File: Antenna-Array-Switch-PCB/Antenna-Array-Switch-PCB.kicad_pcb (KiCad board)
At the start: 2 copper layers, 80 parts, among them J1 Conn_Coaxial, J2 Conn_Coaxial, J3 Conn_Coaxial, J4 Conn_SMA, SW1 TS-1187A-B-A-B, SW2 TS-1187A-B-A-B, U1 PGA-103, U2 TPS22917DBV, U3 TPS22917DBV, U4 PGA-103, U5 TPS22917DBV, U6 PGA-103, U7 SKY13418-485LF, U8 LM1117IMP-3.3, U9 RP2040-Zero

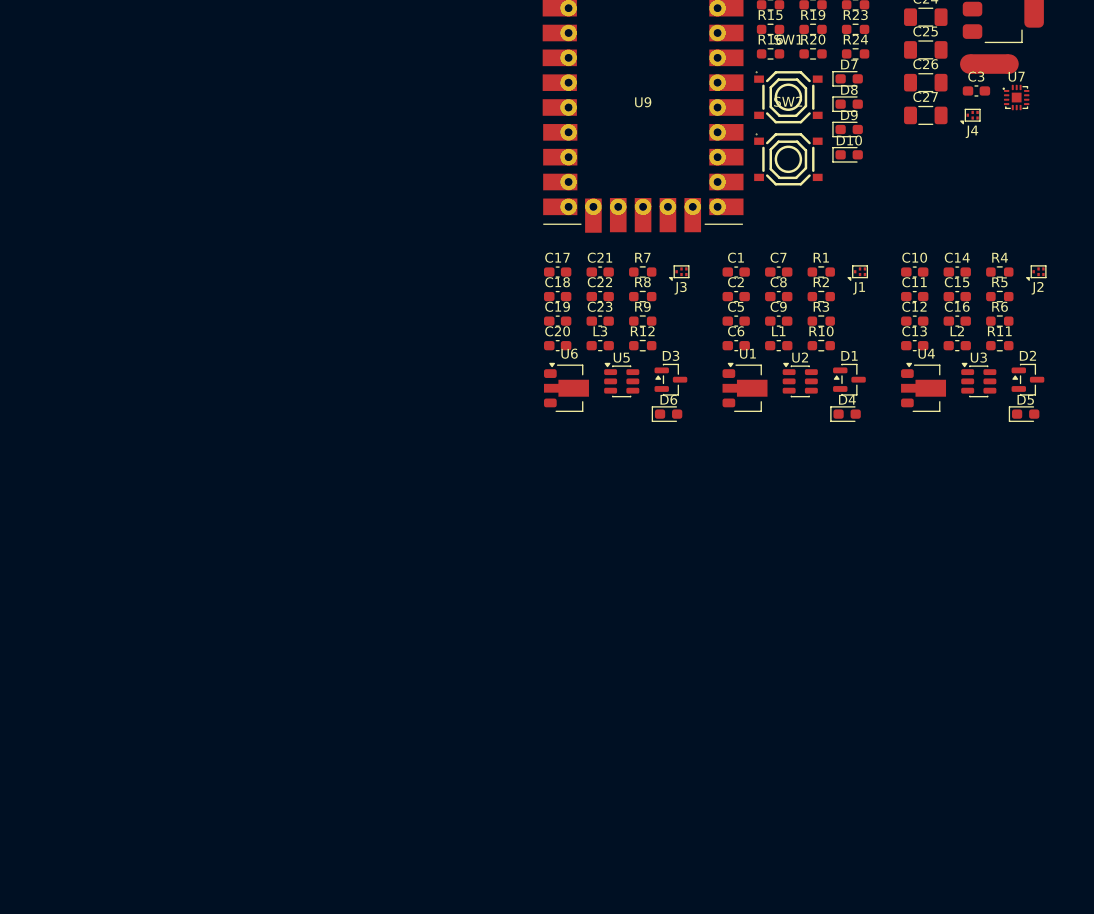
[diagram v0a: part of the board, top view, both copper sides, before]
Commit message: PCB: Layout an LNA segment
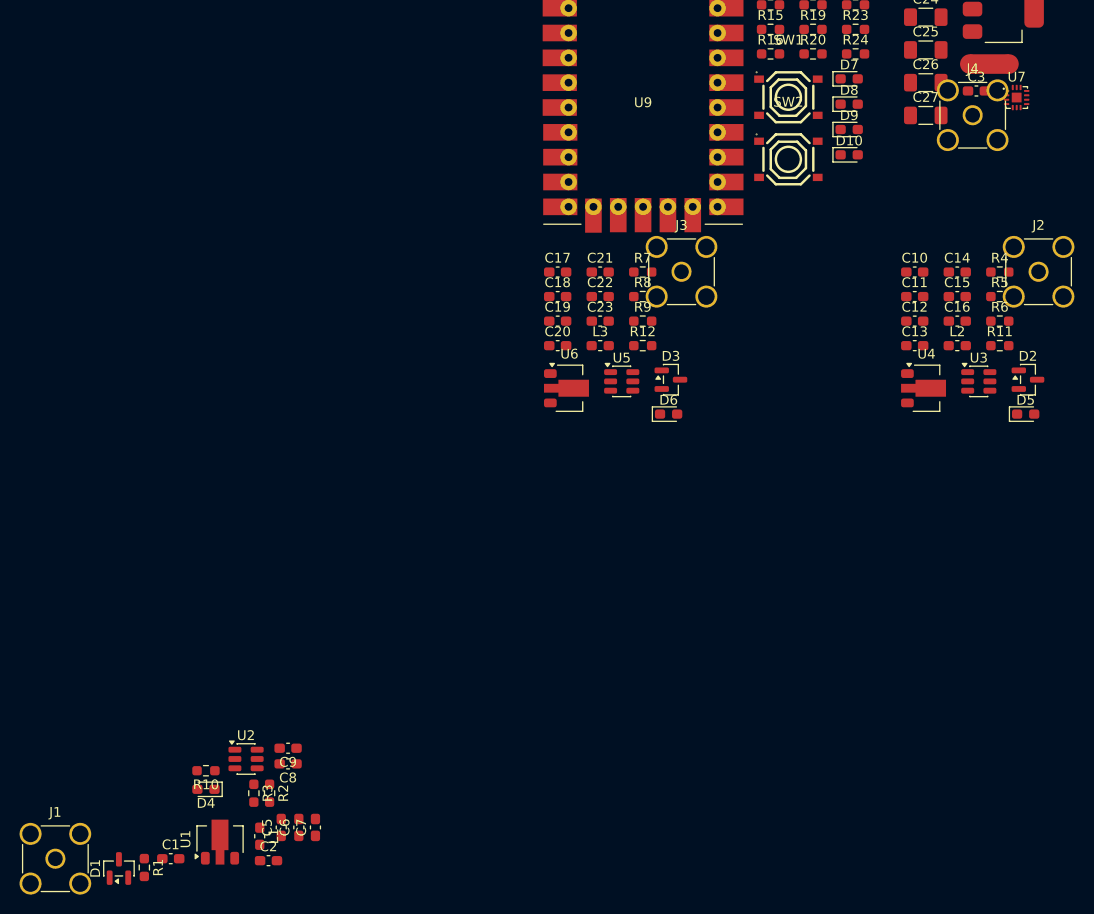
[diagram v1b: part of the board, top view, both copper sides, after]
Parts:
- J1, J2, J3, J4: footprint Filter:Filter_1411-5_1.4x1.1mm -> Connector_Coaxial:SMA_Amphenol_901-144_Vertical
- moved J1 101.9 mm to (63.3, 158.4)
- moved R1 92.2 mm to (72.4, 159.3), turned to -90 degrees
- moved D1 89.9 mm to (69.8, 159.4), turned to 90 degrees
- moved C1 83.3 mm to (75.1, 158.4)
- moved R10 76.5 mm to (78.7, 149.4), turned to 180 degrees
- moved D4 76.0 mm to (78.7, 151.3), turned to 180 degrees
- moved R2 75.9 mm to (85.2, 151.7), turned to -90 degrees
- moved R3 75.5 mm to (83.6, 151.7), turned to -90 degrees
- moved C2 74.9 mm to (85.1, 158.6)
- moved C7 74.0 mm to (89.9, 155.2), turned to 90 degrees
- moved L1 73.0 mm to (84.2, 156.1), turned to -90 degrees
- moved U1 71.0 mm to (80.1, 156.4), turned to 90 degrees
- moved C5 69.6 mm to (86.4, 155.2), turned to 90 degrees
- moved C8 69.3 mm to (87.1, 148.7), turned to 180 degrees
- moved U2 68.6 mm to (82.8, 148.2)
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
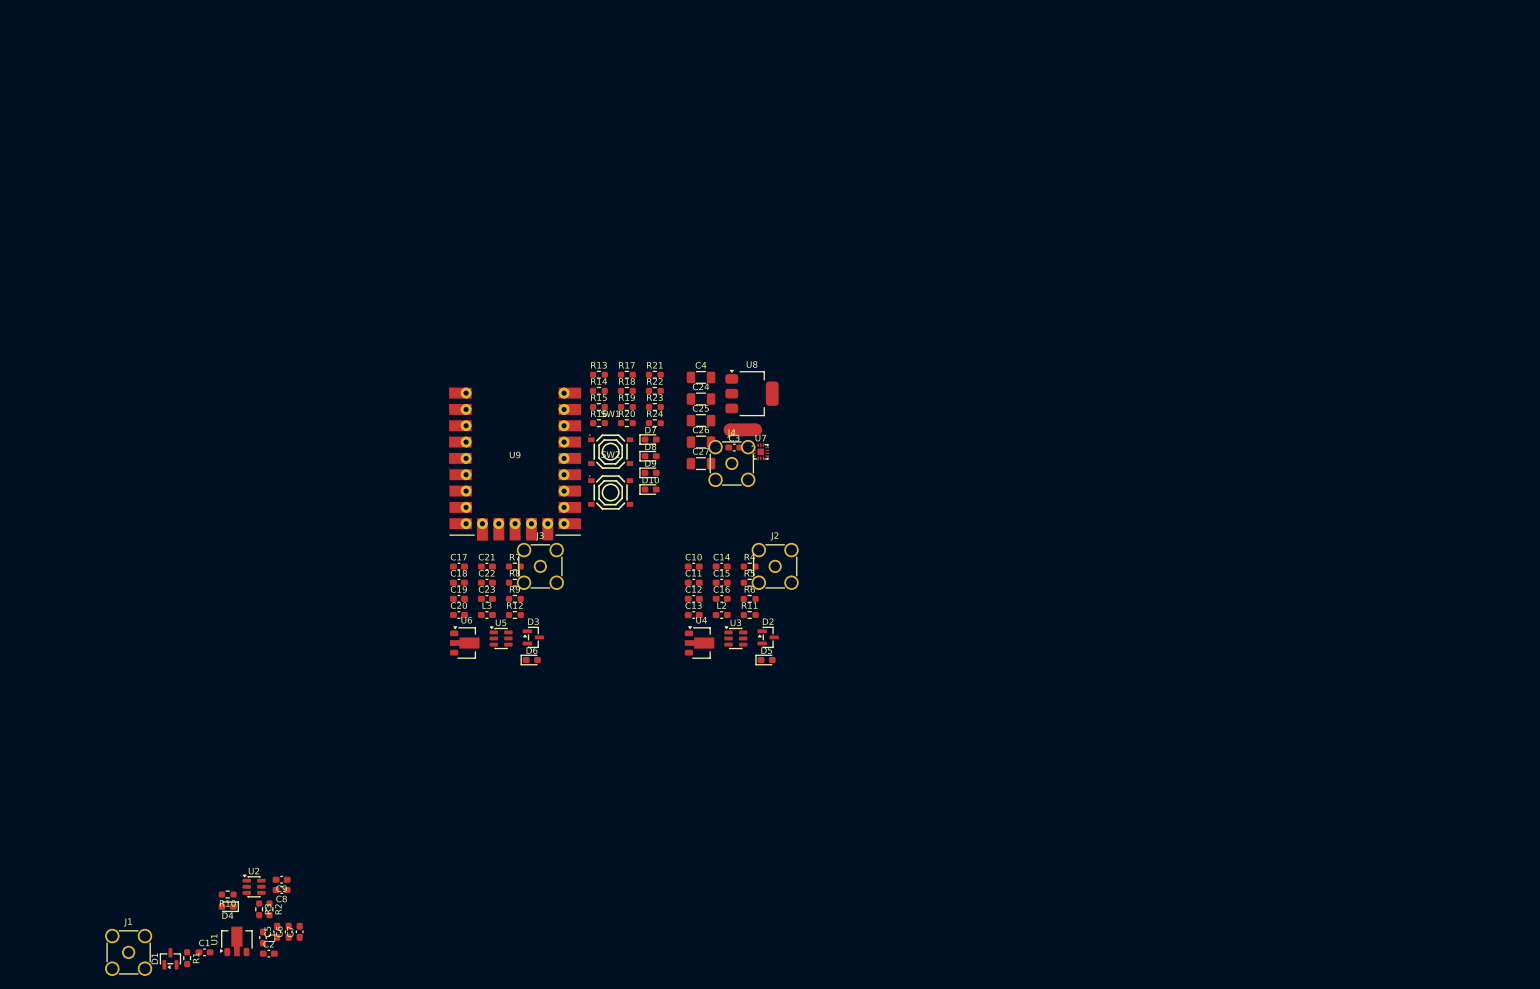
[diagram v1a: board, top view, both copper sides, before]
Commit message: PCB, Docs: Layout, stackup, shielding
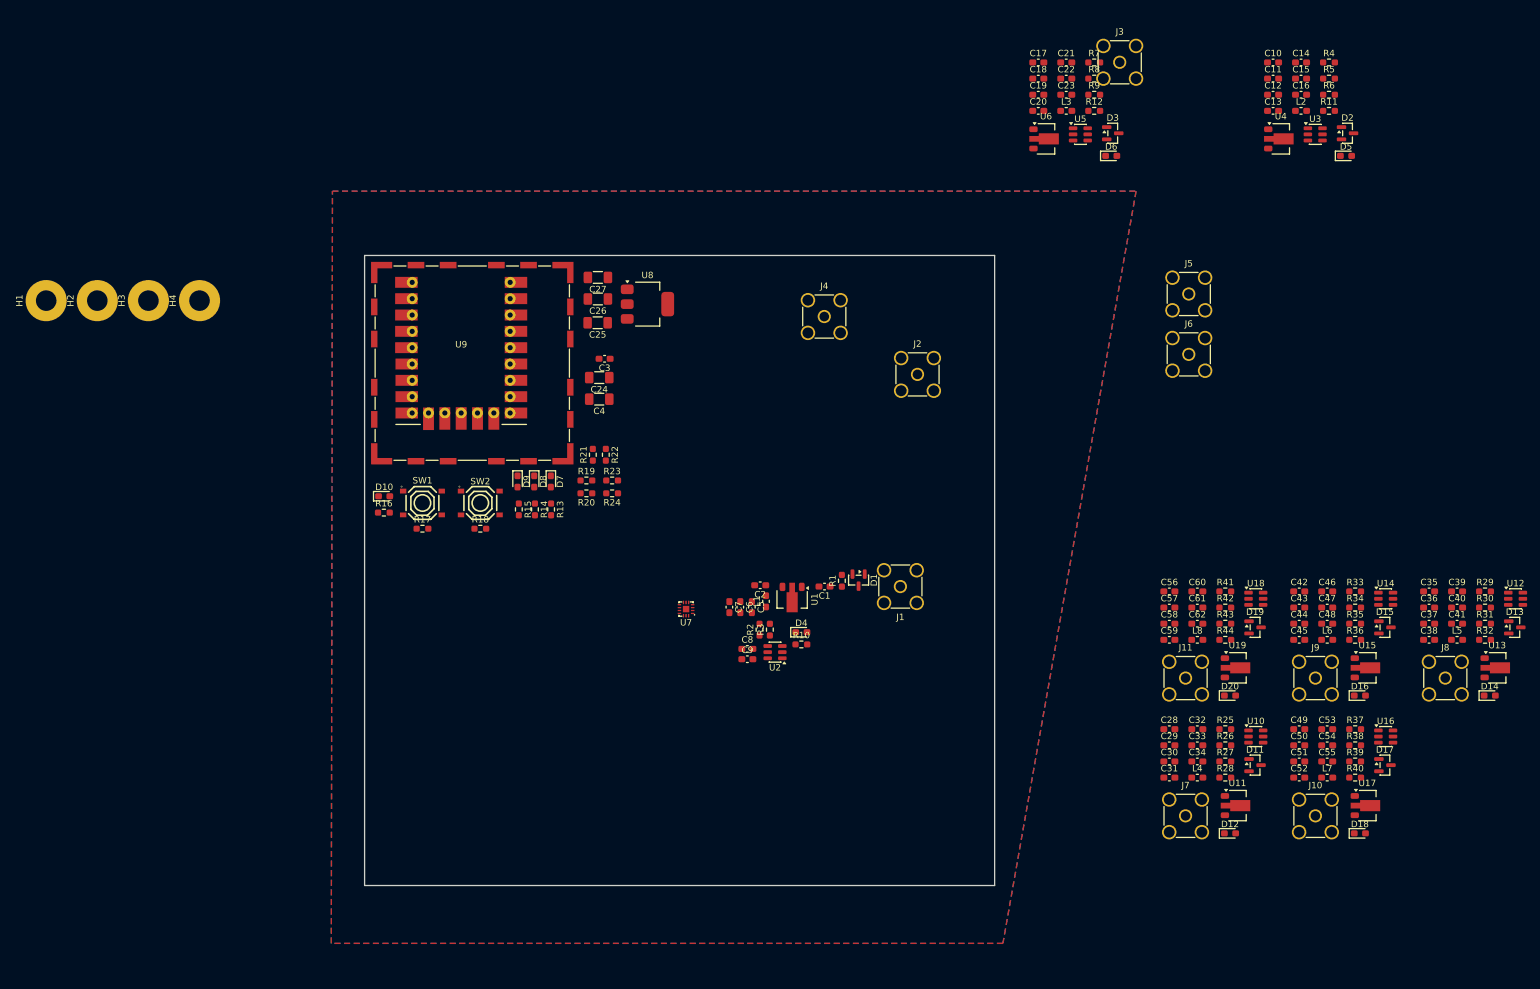
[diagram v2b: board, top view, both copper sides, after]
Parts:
- removed NT1: NetTie_2, NetTie:NetTie-2_SMD_Pad2.0mm
- added C28: 1nF, Capacitor_SMD:C_0603_1608Metric_Pad1.08x0.95mm_HandSolder, F.Cu at (225.2, 123.7)
- added C29: 10nF, Capacitor_SMD:C_0603_1608Metric_Pad1.08x0.95mm_HandSolder, F.Cu at (225.2, 126.2)
- added C30: 1uF, Capacitor_SMD:C_0603_1608Metric_Pad1.08x0.95mm_HandSolder, F.Cu at (225.2, 128.7)
- added C31: 100pF, Capacitor_SMD:C_0603_1608Metric_Pad1.08x0.95mm_HandSolder, F.Cu at (225.2, 131.2)
- added C32: 1nF, Capacitor_SMD:C_0603_1608Metric_Pad1.08x0.95mm_HandSolder, F.Cu at (229.5, 123.7)
- added C33: 1n, Capacitor_SMD:C_0603_1608Metric_Pad1.08x0.95mm_HandSolder, F.Cu at (229.5, 126.2)
- added C34: 10nF, Capacitor_SMD:C_0603_1608Metric_Pad1.08x0.95mm_HandSolder, F.Cu at (229.5, 128.7)
- added C35: 1nF, Capacitor_SMD:C_0603_1608Metric_Pad1.08x0.95mm_HandSolder, F.Cu at (265.6, 102.3)
- added C36: 10nF, Capacitor_SMD:C_0603_1608Metric_Pad1.08x0.95mm_HandSolder, F.Cu at (265.6, 104.8)
- added C37: 1uF, Capacitor_SMD:C_0603_1608Metric_Pad1.08x0.95mm_HandSolder, F.Cu at (265.6, 107.3)
- added C38: 100pF, Capacitor_SMD:C_0603_1608Metric_Pad1.08x0.95mm_HandSolder, F.Cu at (265.6, 109.8)
- added C39: 1nF, Capacitor_SMD:C_0603_1608Metric_Pad1.08x0.95mm_HandSolder, F.Cu at (269.9, 102.3)
- added C40: 1n, Capacitor_SMD:C_0603_1608Metric_Pad1.08x0.95mm_HandSolder, F.Cu at (269.9, 104.8)
- added C41: 10nF, Capacitor_SMD:C_0603_1608Metric_Pad1.08x0.95mm_HandSolder, F.Cu at (269.9, 107.3)
- added C42: 1nF, Capacitor_SMD:C_0603_1608Metric_Pad1.08x0.95mm_HandSolder, F.Cu at (245.4, 102.3)
- added C43: 10nF, Capacitor_SMD:C_0603_1608Metric_Pad1.08x0.95mm_HandSolder, F.Cu at (245.4, 104.8)
- added C44: 1uF, Capacitor_SMD:C_0603_1608Metric_Pad1.08x0.95mm_HandSolder, F.Cu at (245.4, 107.3)
- added C45: 100pF, Capacitor_SMD:C_0603_1608Metric_Pad1.08x0.95mm_HandSolder, F.Cu at (245.4, 109.8)
- added C46: 1nF, Capacitor_SMD:C_0603_1608Metric_Pad1.08x0.95mm_HandSolder, F.Cu at (249.7, 102.3)
- added C47: 1n, Capacitor_SMD:C_0603_1608Metric_Pad1.08x0.95mm_HandSolder, F.Cu at (249.7, 104.8)
- added C48: 10nF, Capacitor_SMD:C_0603_1608Metric_Pad1.08x0.95mm_HandSolder, F.Cu at (249.7, 107.3)
- added C49: 1nF, Capacitor_SMD:C_0603_1608Metric_Pad1.08x0.95mm_HandSolder, F.Cu at (245.4, 123.7)
- added C50: 10nF, Capacitor_SMD:C_0603_1608Metric_Pad1.08x0.95mm_HandSolder, F.Cu at (245.4, 126.2)
- added C51: 1uF, Capacitor_SMD:C_0603_1608Metric_Pad1.08x0.95mm_HandSolder, F.Cu at (245.4, 128.7)
- added C52: 100pF, Capacitor_SMD:C_0603_1608Metric_Pad1.08x0.95mm_HandSolder, F.Cu at (245.4, 131.2)
- added C53: 1nF, Capacitor_SMD:C_0603_1608Metric_Pad1.08x0.95mm_HandSolder, F.Cu at (249.7, 123.7)
- added C54: 1n, Capacitor_SMD:C_0603_1608Metric_Pad1.08x0.95mm_HandSolder, F.Cu at (249.7, 126.2)
- added C55: 10nF, Capacitor_SMD:C_0603_1608Metric_Pad1.08x0.95mm_HandSolder, F.Cu at (249.7, 128.7)
- added C56: 1nF, Capacitor_SMD:C_0603_1608Metric_Pad1.08x0.95mm_HandSolder, F.Cu at (225.2, 102.3)
- added C57: 10nF, Capacitor_SMD:C_0603_1608Metric_Pad1.08x0.95mm_HandSolder, F.Cu at (225.2, 104.8)
- added C58: 1uF, Capacitor_SMD:C_0603_1608Metric_Pad1.08x0.95mm_HandSolder, F.Cu at (225.2, 107.3)
- added C59: 100pF, Capacitor_SMD:C_0603_1608Metric_Pad1.08x0.95mm_HandSolder, F.Cu at (225.2, 109.8)
- added C60: 1nF, Capacitor_SMD:C_0603_1608Metric_Pad1.08x0.95mm_HandSolder, F.Cu at (229.5, 102.3)
- added C61: 1n, Capacitor_SMD:C_0603_1608Metric_Pad1.08x0.95mm_HandSolder, F.Cu at (229.5, 104.8)
- added C62: 10nF, Capacitor_SMD:C_0603_1608Metric_Pad1.08x0.95mm_HandSolder, F.Cu at (229.5, 107.3)
- added D11: BAV99, Package_TO_SOT_SMD:SOT-23, F.Cu at (238.5, 129.3)
- added D12: LED, LED_SMD:LED_0603_1608Metric_Pad1.05x0.95mm_HandSolder, F.Cu at (234.6, 139.9)
- added D13: BAV99, Package_TO_SOT_SMD:SOT-23, F.Cu at (278.9, 107.8)
- added D14: LED, LED_SMD:LED_0603_1608Metric_Pad1.05x0.95mm_HandSolder, F.Cu at (275.0, 118.5)
- added D15: BAV99, Package_TO_SOT_SMD:SOT-23, F.Cu at (258.7, 107.8)
- added D16: LED, LED_SMD:LED_0603_1608Metric_Pad1.05x0.95mm_HandSolder, F.Cu at (254.8, 118.5)
- added D17: BAV99, Package_TO_SOT_SMD:SOT-23, F.Cu at (258.7, 129.3)
- added D18: LED, LED_SMD:LED_0603_1608Metric_Pad1.05x0.95mm_HandSolder, F.Cu at (254.8, 139.9)
- added D19: BAV99, Package_TO_SOT_SMD:SOT-23, F.Cu at (238.5, 107.8)
- added D20: LED, LED_SMD:LED_0603_1608Metric_Pad1.05x0.95mm_HandSolder, F.Cu at (234.6, 118.5)
- added H1: MountingHole_Pad, MountingHole:MountingHole_3.2mm_M3_Pad, F.Cu at (50.5, 57.0)
- added H2: MountingHole_Pad, MountingHole:MountingHole_3.2mm_M3_Pad, F.Cu at (58.4, 57.0)
- added H3: MountingHole_Pad, MountingHole:MountingHole_3.2mm_M3_Pad, F.Cu at (66.4, 57.0)
- added H4: MountingHole_Pad, MountingHole:MountingHole_3.2mm_M3_Pad, F.Cu at (74.3, 57.0)
- added J10: Conn_Coaxial, Connector_Coaxial:SMA_Amphenol_901-144_Vertical, F.Cu at (247.9, 137.2)
- added J11: Conn_Coaxial, Connector_Coaxial:SMA_Amphenol_901-144_Vertical, F.Cu at (227.7, 115.7)
- added J12: RFShield_OnePiece, RF_Shielding:Wuerth_36103305_30x30mm, F.Cu at (116.8, 66.8)
- added J5: Conn_SMA, Connector_Coaxial:SMA_Amphenol_901-144_Vertical, F.Cu at (228.2, 56.0)
- added J6: Conn_SMA, Connector_Coaxial:SMA_Amphenol_901-144_Vertical, F.Cu at (228.2, 65.4)
- added J7: Conn_Coaxial, Connector_Coaxial:SMA_Amphenol_901-144_Vertical, F.Cu at (227.7, 137.2)
- added J8: Conn_Coaxial, Connector_Coaxial:SMA_Amphenol_901-144_Vertical, F.Cu at (268.1, 115.7)
- added J9: Conn_Coaxial, Connector_Coaxial:SMA_Amphenol_901-144_Vertical, F.Cu at (247.9, 115.7)
- added L4: 220nH, Inductor_SMD:L_0603_1608Metric_Pad1.05x0.95mm_HandSolder, F.Cu at (229.5, 131.2)
- added L5: 220nH, Inductor_SMD:L_0603_1608Metric_Pad1.05x0.95mm_HandSolder, F.Cu at (269.9, 109.8)
- added L6: 220nH, Inductor_SMD:L_0603_1608Metric_Pad1.05x0.95mm_HandSolder, F.Cu at (249.7, 109.8)
- added L7: 220nH, Inductor_SMD:L_0603_1608Metric_Pad1.05x0.95mm_HandSolder, F.Cu at (249.7, 131.2)
- added L8: 220nH, Inductor_SMD:L_0603_1608Metric_Pad1.05x0.95mm_HandSolder, F.Cu at (229.5, 109.8)
- added R25: 1M, Resistor_SMD:R_0603_1608Metric_Pad0.98x0.95mm_HandSolder, F.Cu at (233.9, 123.7)
- added R26: 10k, Resistor_SMD:R_0603_1608Metric_Pad0.98x0.95mm_HandSolder, F.Cu at (233.9, 126.2)
- added R27: 10, Resistor_SMD:R_0603_1608Metric_Pad0.98x0.95mm_HandSolder, F.Cu at (233.9, 128.7)
- added R28: 10, Resistor_SMD:R_0603_1608Metric_Pad0.98x0.95mm_HandSolder, F.Cu at (233.9, 131.2)
- added R29: 1M, Resistor_SMD:R_0603_1608Metric_Pad0.98x0.95mm_HandSolder, F.Cu at (274.3, 102.3)
- added R30: 10k, Resistor_SMD:R_0603_1608Metric_Pad0.98x0.95mm_HandSolder, F.Cu at (274.3, 104.8)
- added R31: 10, Resistor_SMD:R_0603_1608Metric_Pad0.98x0.95mm_HandSolder, F.Cu at (274.3, 107.3)
- added R32: 10, Resistor_SMD:R_0603_1608Metric_Pad0.98x0.95mm_HandSolder, F.Cu at (274.3, 109.8)
- added R33: 1M, Resistor_SMD:R_0603_1608Metric_Pad0.98x0.95mm_HandSolder, F.Cu at (254.1, 102.3)
- added R34: 10k, Resistor_SMD:R_0603_1608Metric_Pad0.98x0.95mm_HandSolder, F.Cu at (254.1, 104.8)
- added R35: 10, Resistor_SMD:R_0603_1608Metric_Pad0.98x0.95mm_HandSolder, F.Cu at (254.1, 107.3)
- added R36: 10, Resistor_SMD:R_0603_1608Metric_Pad0.98x0.95mm_HandSolder, F.Cu at (254.1, 109.8)
- added R37: 1M, Resistor_SMD:R_0603_1608Metric_Pad0.98x0.95mm_HandSolder, F.Cu at (254.1, 123.7)
- added R38: 10k, Resistor_SMD:R_0603_1608Metric_Pad0.98x0.95mm_HandSolder, F.Cu at (254.1, 126.2)
- added R39: 10, Resistor_SMD:R_0603_1608Metric_Pad0.98x0.95mm_HandSolder, F.Cu at (254.1, 128.7)
- added R40: 10, Resistor_SMD:R_0603_1608Metric_Pad0.98x0.95mm_HandSolder, F.Cu at (254.1, 131.2)
- added R41: 1M, Resistor_SMD:R_0603_1608Metric_Pad0.98x0.95mm_HandSolder, F.Cu at (233.9, 102.3)
- added R42: 10k, Resistor_SMD:R_0603_1608Metric_Pad0.98x0.95mm_HandSolder, F.Cu at (233.9, 104.8)
- added R43: 10, Resistor_SMD:R_0603_1608Metric_Pad0.98x0.95mm_HandSolder, F.Cu at (233.9, 107.3)
- added R44: 10, Resistor_SMD:R_0603_1608Metric_Pad0.98x0.95mm_HandSolder, F.Cu at (233.9, 109.8)
- added U10: TPS22917DBV, Package_TO_SOT_SMD:SOT-23-6, F.Cu at (238.6, 124.8)
- added U11: PGA-103, Package_TO_SOT_SMD:SOT-89-3, F.Cu at (235.8, 135.6)
- added U12: TPS22917DBV, Package_TO_SOT_SMD:SOT-23-6, F.Cu at (279.0, 103.4)
- added U13: PGA-103, Package_TO_SOT_SMD:SOT-89-3, F.Cu at (276.2, 114.1)
- added U14: TPS22917DBV, Package_TO_SOT_SMD:SOT-23-6, F.Cu at (258.8, 103.4)
- added U15: PGA-103, Package_TO_SOT_SMD:SOT-89-3, F.Cu at (256.0, 114.1)
- added U16: TPS22917DBV, Package_TO_SOT_SMD:SOT-23-6, F.Cu at (258.8, 124.8)
- added U17: PGA-103, Package_TO_SOT_SMD:SOT-89-3, F.Cu at (256.0, 135.6)
- added U18: TPS22917DBV, Package_TO_SOT_SMD:SOT-23-6, F.Cu at (238.6, 103.4)
- added U19: PGA-103, Package_TO_SOT_SMD:SOT-89-3, F.Cu at (235.8, 114.1)
- moved J1 132.8 mm to (183.3, 101.5), turned to 180 degrees
- moved D1 122.2 mm to (176.8, 100.5), turned to -90 degrees
- moved C11 119.5 mm to (241.3, 22.5)
- moved C12 119.5 mm to (241.3, 25.0)
- moved C15 119.5 mm to (245.7, 22.5)
- moved C16 119.5 mm to (245.7, 25.0)
- moved D3 119.5 mm to (216.4, 31.0)
- moved R8 119.5 mm to (213.5, 22.5)
- moved R9 119.5 mm to (213.5, 25.0)
- moved U6 119.5 mm to (206.0, 31.9)
- moved C10 119.5 mm to (241.3, 20.0)
- moved C13 119.5 mm to (241.3, 27.5)
- moved C14 119.5 mm to (245.7, 20.0)
- moved C17 119.5 mm to (204.8, 20.0)
- moved C18 119.5 mm to (204.8, 22.5)
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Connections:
- D4 pad 1: GNDD -> GNDA
- D5 pad 1: GNDD -> GNDA
- D6 pad 1: GNDD -> GNDA
- R13 pad 2: GNDD -> GNDA
- R14 pad 2: GNDD -> GNDA
- R15 pad 2: GNDD -> GNDA
- R16 pad 2: GNDD -> GNDA
- R17 pad 2: GNDD -> GNDA
- R18 pad 2: GNDD -> GNDA
- U7 pad 1: unconnected-(U7-RF5-Pad1) -> /AntennaBranch4/LNA_RF_OUTPUT
- U7 pad 10: unconnected-(U7-RF4-Pad10) -> /AntennaBranch3/LNA_RF_OUTPUT
- U7 pad 11: unconnected-(U7-RF6-Pad11) -> /AntennaBranch5/LNA_RF_OUTPUT
- U7 pad 12: unconnected-(U7-RF8-Pad12) -> /AntennaBranch7/LNA_RF_OUTPUT
- U7 pad 14: unconnected-(U7-RF7-Pad14) -> /AntennaBranch6/LNA_RF_OUTPUT
- U9 pad 2: GNDD -> GNDA
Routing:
- added copper zone on B.Cu, net GNDA
- added copper zone on F.Cu, net GNDA
- added copper zone on In1.Cu, net GNDA
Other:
- board outline added: 98 x 98 mm
- copper layers 2 -> 4

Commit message: PCB: Layout - position connectors for autoplacement
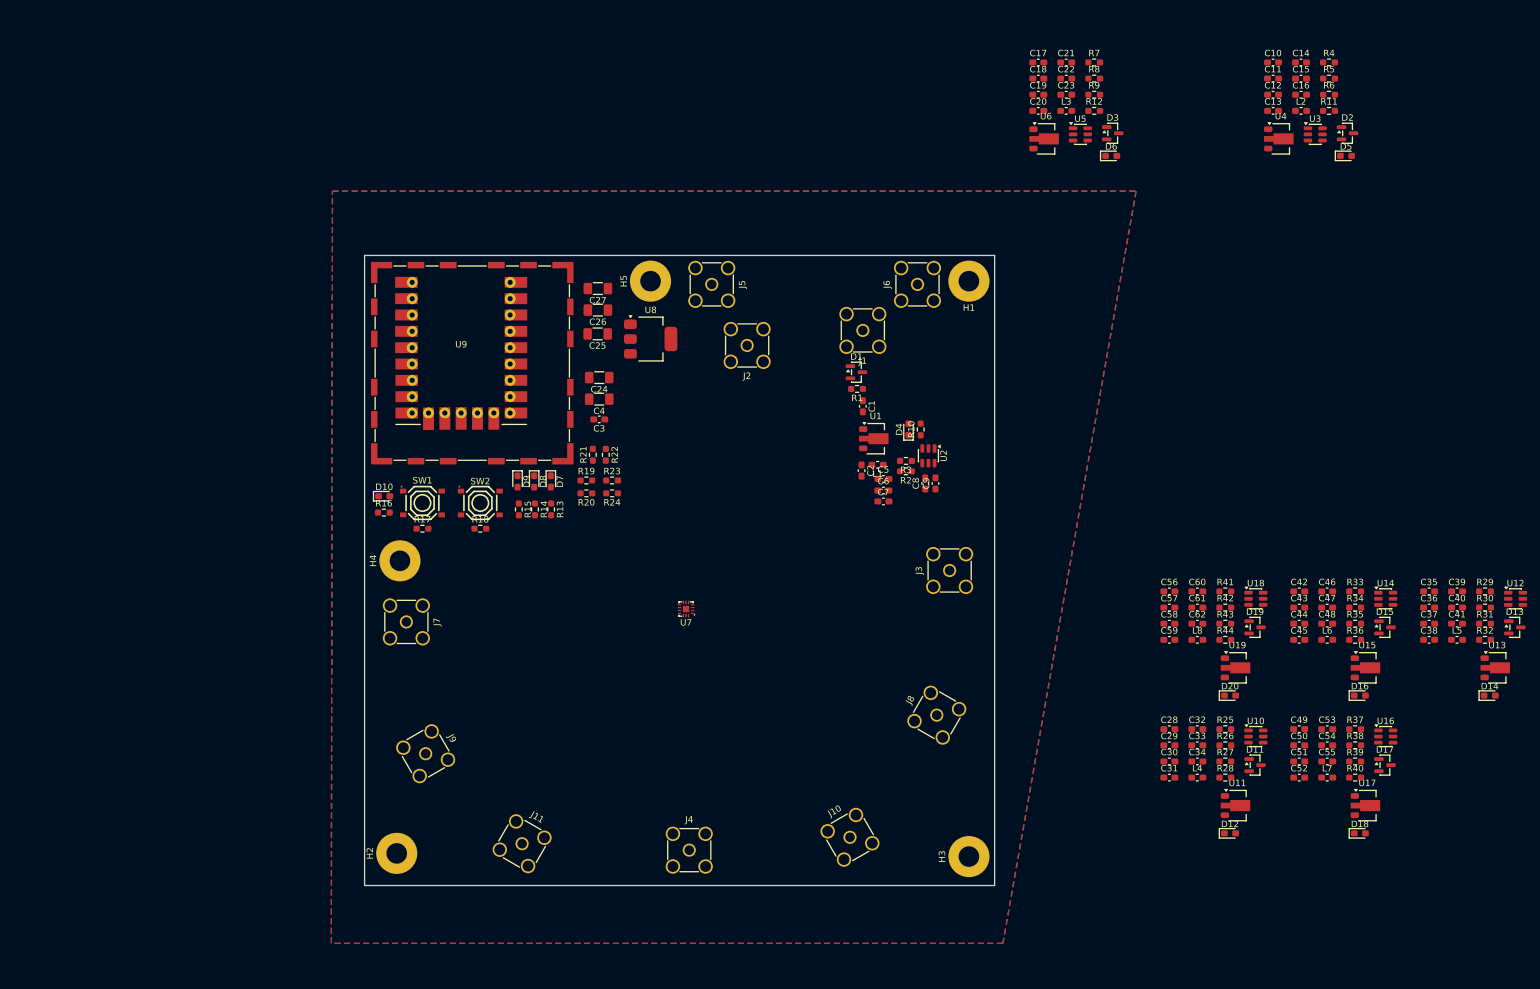
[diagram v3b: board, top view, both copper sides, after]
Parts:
- added H5: MountingHole_Pad, MountingHole:MountingHole_3.2mm_M3_Pad, F.Cu at (144.5, 54.0)
- moved H3 154.2 mm to (194.0, 143.5)
- moved H1 143.6 mm to (194.0, 54.0), turned to 180 degrees
- moved J9 138.9 mm to (109.5, 127.5), turned to -60 degrees
- moved J7 124.9 mm to (106.5, 107.0), turned to -90 degrees
- moved J11 106.4 mm to (124.5, 141.5), turned to -30 degrees
- moved H2 97.8 mm to (105.0, 143.0)
- moved J4 85.6 mm to (150.5, 142.5)
- moved J3 83.4 mm to (191.0, 99.0), turned to 90 degrees
- moved J8 79.3 mm to (189.0, 121.5), turned to 60 degrees
- moved J5 74.2 mm to (154.0, 54.5), turned to -90 degrees
- moved J10 72.5 mm to (175.5, 140.5), turned to 30 degrees
- moved H4 51.1 mm to (105.5, 97.5)
- moved J6 43.6 mm to (186.0, 54.5), turned to 90 degrees
- moved J1 40.3 mm to (177.5, 61.7)
- moved C9 40.0 mm to (188.8, 85.5), turned to 90 degrees
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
